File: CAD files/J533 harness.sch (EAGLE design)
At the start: 7 parts, among them J1 From car, J2 to J533 module, J3 From car, J4 to J533 module

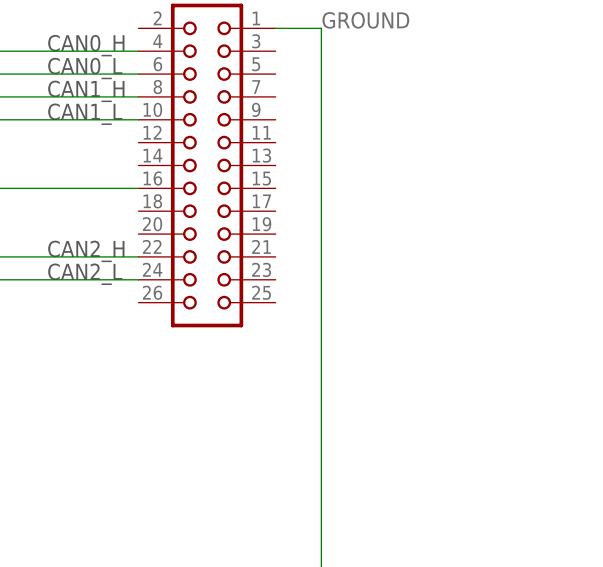
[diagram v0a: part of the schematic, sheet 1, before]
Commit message: Fixed critical fault
Missing CAN termination enable jumper
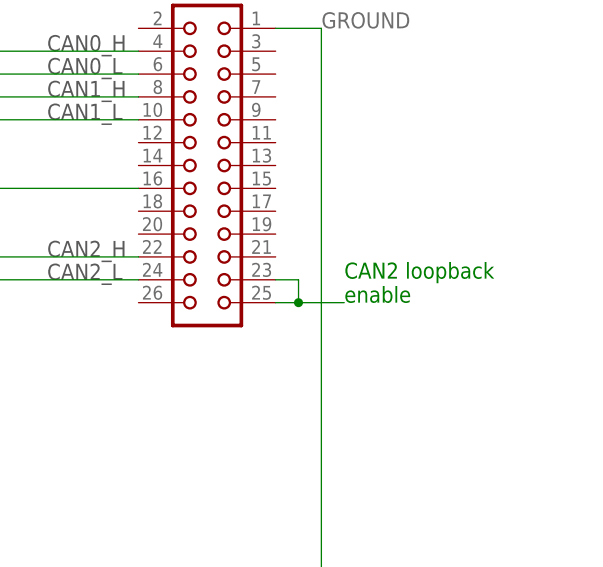
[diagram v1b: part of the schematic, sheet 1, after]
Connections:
- new net N$4: MOLEX_IGRID_TO_COMMA_RELAY1.23, MOLEX_IGRID_TO_COMMA_RELAY1.25
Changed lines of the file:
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@@
 <text x="142.24" y="71.12" size="1.778" layer="95">CAN_EXTENDED_LOW</text>
 <text x="142.24" y="45.72" size="1.778" layer="95">CAN_EXTENDED_HIGH</text>
+<text x="167.64" y="129.54" size="1.778" layer="91">CAN2 loopback
+enable</text>
 </plain>
 <instances>
@@
 </segment>
 </net>
+<net name="N$4" class="0">
+<segment>
+<pinref part="MOLEX_IGRID_TO_COMMA_RELAY1" gate="A" pin="25"/>
+<wire x1="160.02" y1="129.54" x2="162.56" y2="129.54" width="0.1524" layer="91"/>
+<wire x1="162.56" y1="129.54" x2="162.56" y2="132.08" width="0.1524" layer="91"/>
+<pinref part="MOLEX_IGRID_TO_COMMA_RELAY1" gate="A" pin="23"/>
+<wire x1="162.56" y1="132.08" x2="160.02" y2="132.08" width="0.1524" layer="91"/>
+<wire x1="167.64" y1="129.54" x2="162.56" y2="129.54" width="0.1524" layer="91"/>
+<junction x="162.56" y="129.54"/>
+</segment>
+</net>
